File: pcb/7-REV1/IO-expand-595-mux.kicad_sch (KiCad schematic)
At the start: 58 parts, among them U10 LM358_DFN, U11 LM358_DFN, U12 LM358_DFN, U13 LM358_DFN, U2 74LVC8T245BQ, U402 CD4067, U503 74HCT245BQ, U9 LM358_DFN

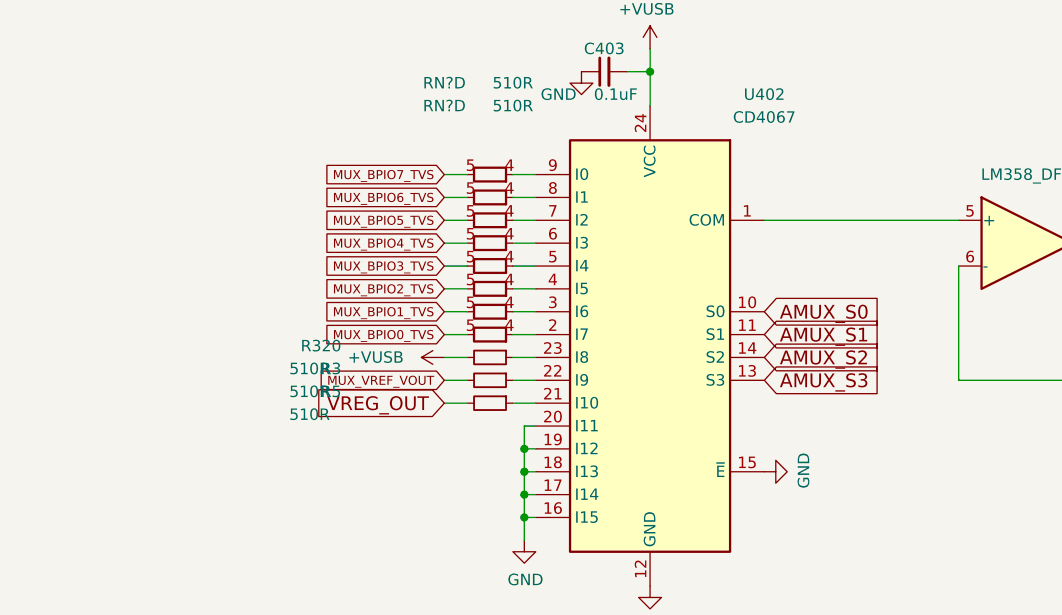
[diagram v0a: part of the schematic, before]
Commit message: Move CURRENT_DETECT back to AMUX
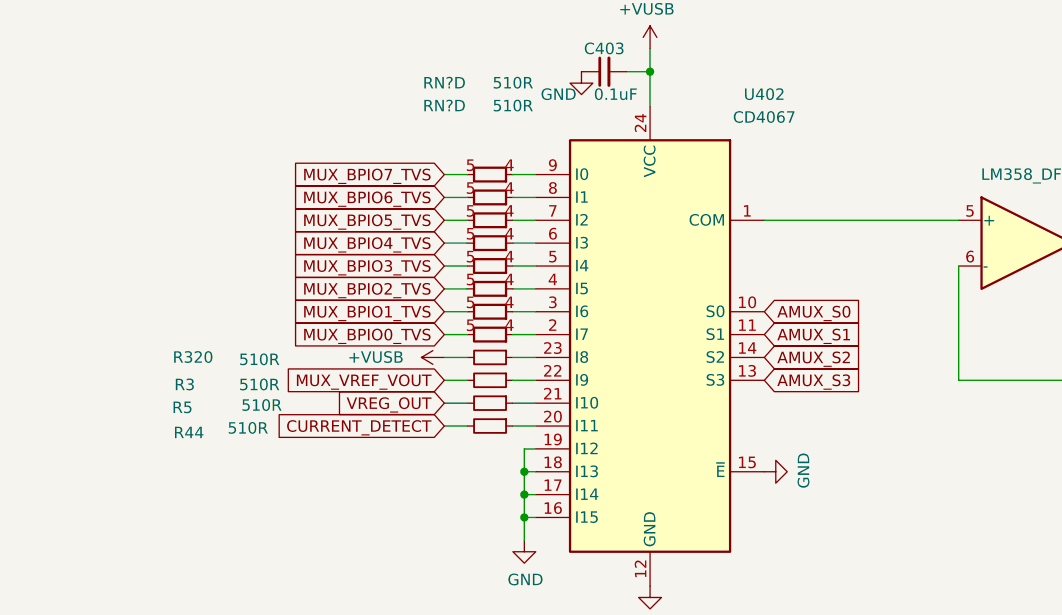
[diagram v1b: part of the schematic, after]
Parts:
- added R44: 510R, Resistor_SMD:R_0402_1005Metric, symbol Device:R_Small
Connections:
- net GND: no longer U402.20 (I11)
- new net: R44.1, U402.20 (I11)
- new net CURRENT_DETECT: R44.2
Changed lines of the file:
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@@
 	)
 	(junction
-		(at 246.38 170.18)
-		(diameter 0)
-		(color 0 0 0 0)
-	)
-	(junction
 		(at 76.2 175.26)
 		(diameter 0)
@@
 	(wire
 		(pts
+			(xy 237.49 167.64) (xy 240.03 167.64)
+		)
+		(stroke
+			(width 0)
+			(type default)
+		)
+	)
+	(wire
+		(pts
 			(xy 237.49 142.24) (xy 240.03 142.24)
 		)
@@
 	(wire
 		(pts
-			(xy 246.38 167.64) (xy 246.38 170.18)
-		)
-		(stroke
-			(width 0)
-			(type default)
-		)
-	)
-	(wire
-		(pts
 			(xy 245.11 162.56) (xy 247.65 162.56)
 		)
@@
 	(wire
 		(pts
-			(xy 246.38 167.64) (xy 247.65 167.64)
-		)
-		(stroke
-			(width 0)
-			(type default)
-		)
-	)
-	(wire
-		(pts
 			(xy 41.91 78.74) (xy 60.96 78.74)
 		)
@@
 	(wire
 		(pts
+			(xy 245.11 167.64) (xy 247.65 167.64)
+		)
+		(stroke
+			(width 0)
+			(type default)
+		)
+	)
+	(wire
+		(pts
 			(xy 142.24 121.92) (xy 157.48 121.92)
 		)
@@
 		(effects
 			(font
-				(size 1 1)
+				(size 1.27 1.27)
 			)
 			(justify right)
@@
 		(effects
 			(font
-				(size 1.524 1.524)
+				(size 1.27 1.27)
 			)
 			(justify left)
@@
 		(effects
 			(font
-				(size 1.524 1.524)
+				(size 1.27 1.27)
 			)
 			(justify left)
@@
 		(effects
 			(font
-				(size 1 1)
+				(size 1.27 1.27)
 			)
 			(justify right)
@@
 		(effects
 			(font
-				(size 1 1)
+				(size 1.27 1.27)
 			)
 			(justify right)
@@
 		(effects
 			(font
-				(size 1.524 1.524)
+				(size 1.27 1.27)
 			)
 			(justify right)
@@
 		(effects
 			(font
-				(size 1 1)
+				(size 1.27 1.27)
 			)
 			(justify right)
@@
 		(effects
 			(font
-				(size 1 1)
+				(size 1.27 1.27)
 			)
 			(justify right)
@@
 		(effects
 			(font
-				(size 1 1)
+				(size 1.27 1.27)
 			)
 			(justify right)
@@
 		)
 	)
+	(global_label "CURRENT_DETECT"
+		(shape input)
+		(at 237.49 167.64 180)
+		(fields_autoplaced yes)
+		(effects
+			(font
+				(size 1.27 1.27)
+			)
+			(justify right)
+		)
+		(property "Intersheetrefs" "${INTERSHEET_REFS}"
+			(at 218.8306 167.64 0)
+			(effects
+				(font
+					(size 1.27 1.27)
+				)
+				(justify right)
+				(hide yes)
+			)
+		)
+	)
 	(global_label "BPIO7_TVS"
 		(shape input)
@@
 		(effects
 			(font
-				(size 1 1)
+				(size 1.27 1.27)
 			)
 			(justify right)
@@
 		(effects
 			(font
-				(size 1 1)
+				(size 1.27 1.27)
 			)
 			(justify right)
@@
 		(effects
 			(font
-				(size 1.524 1.524)
+				(size 1.27 1.27)
 			)
 			(justify left)
@@
 		(effects
 			(font
-				(size 1 1)
+				(size 1.27 1.27)
 			)
 			(justify right)
@@
 		(effects
 			(font
-				(size 1.524 1.524)
+				(size 1.27 1.27)
 			)
 			(justify left)
@@
 		(dnp no)
 		(property "Reference" "R320"
-			(at 226.06 158.75 90)
+			(at 211.836 160.02 90)
 			(effects
 				(font
@@
 		)
 		(property "Value" "510R"
-			(at 224.79 161.29 90)
+			(at 219.202 160.274 90)
 			(effects
 				(font
@@
 	)
 	(symbol
+		(lib_id "Device:R_Small")
+		(at 242.57 167.64 270)
+		(unit 1)
+		(exclude_from_sim no)
+		(in_bom yes)
+		(on_board yes)
+		(dnp no)
+		(property "Reference" "R44"
+			(at 210.82 168.402 90)
+			(effects
+				(font
+					(size 1.27 1.27)
+				)
+				(justify right)
+			)
+		)
+		(property "Value" "510R"
+			(at 217.932 167.894 90)
+			(effects
+				(font
+					(size 1.27 1.27)
+				)
+				(justify right)
+			)
+		)
+		(property "Footprint" "Resistor_SMD:R_0402_1005Metric"
+			(at 242.57 167.64 0)
+			(effects
+				(font
+					(size 1.27 1.27)
+				)
+				(hide yes)
+			)
+		)
+		(property "Datasheet" "~"
+			(at 242.57 167.64 0)
+			(effects
+				(font
+					(size 1.27 1.27)
+				)
+				(hide yes)
+			)
+		)
+		(property "Description" ""
+			(at 242.57 167.64 0)
+			(effects
+				(font
+					(size 1.27 1.27)
+				)
+				(hide yes)
+			)
+		)
+		(property "RMB" "0.004864"
+			(at 242.57 167.64 0)
+			(effects
+				(font
+					(size 1.27 1.27)
+				)
+				(hide yes)
+			)
+		)
+		(property "Supplier" "https://item.szlcsc.com/61542.html"
+			(at 242.57 167.64 0)
+			(effects
+				(font
+					(size 1.27 1.27)
+				)
+				(hide yes)
+			)
+		)
+		(pin "1"
+		)
+		(pin "2"
+		)
+		(instances
+			(project "7-REV1"
+				(path "/1f56410a-eaac-4444-b0f7-cfd3531e22ac/00000000-0000-0000-0000-000060e58ecc"
+					(reference "R44")
+					(unit 1)
+				)
+			)
+		)
+	)
+	(symbol
 		(lib_id "Amplifier_Operational:LM358_DFN")
 		(at 149.86 177.8 0)
@@
 		(dnp no)
 		(property "Reference" "R3"
-			(at 226.06 161.29 90)
+			(at 209.804 163.068 90)
 			(effects
 				(font
@@
 		)
 		(property "Value" "510R"
-			(at 224.79 163.83 90)
+			(at 219.202 163.068 90)
 			(effects
 				(font
@@
 		(dnp no)
 		(property "Reference" "R5"
-			(at 226.06 163.83 90)
+			(at 209.55 165.608 90)
 			(effects
 				(font
@@
 		)
 		(property "Value" "510R"
-			(at 224.79 166.37 90)
+			(at 219.456 165.354 90)
 			(effects
 				(font

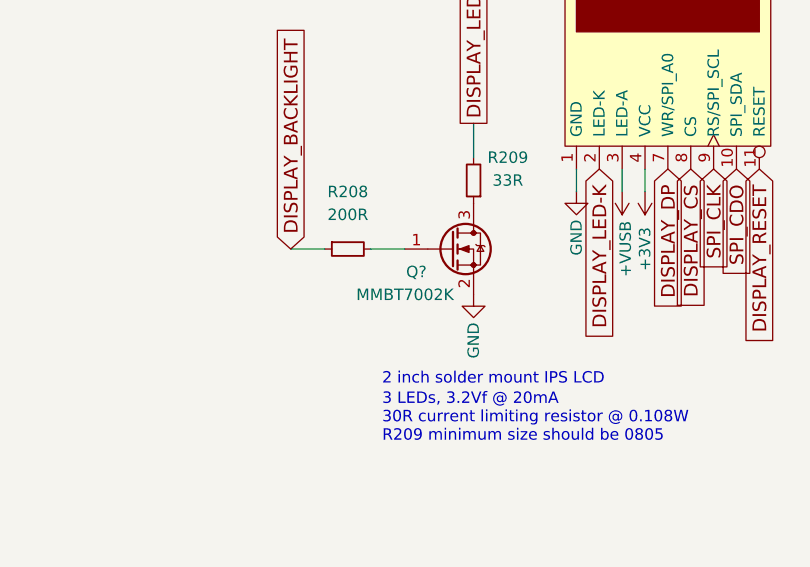
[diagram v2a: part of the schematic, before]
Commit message: replace one more MMBT7002K in SOT-23 with 2N7002T in SOT-523 (display led backlight)
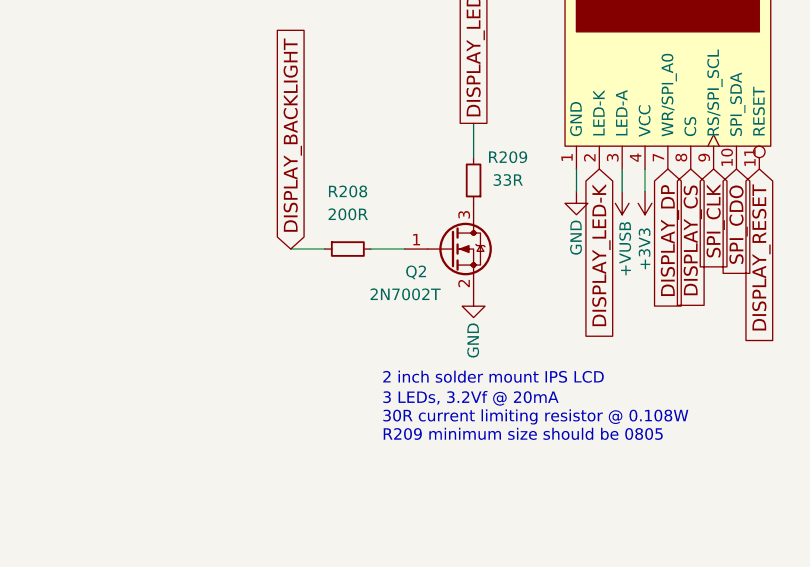
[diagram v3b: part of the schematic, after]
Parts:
- removed Q?: MMBT7002K, Package_TO_SOT_SMD:SOT-23, symbol Transistor_FET:BSS138
- added Q2: 2N7002T, Package_TO_SOT_SMD:SOT-523, symbol Transistor_FET:BSS138
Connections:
- net GND: now also Q2.2 (S)
- net at R208.2: now also Q2.1 (G)
- net at R209.1: now also Q2.3 (D)
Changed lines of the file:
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@@
-	)
-	(symbol
-		(lib_id "Transistor_FET:BSS138")
-		(at 344.17 69.85 0)
-		(unit 1)
-		(exclude_from_sim no)
-		(in_bom yes)
-		(on_board yes)
-		(dnp no)
-		(property "Reference" "Q?"
-			(at 340.36 72.39 0)
-			(effects
-				(font
-					(size 1.27 1.27)
-				)
-			)
-		)
-		(property "Value" "MMBT7002K"
-			(at 339.09 74.93 0)
-			(effects
-				(font
-					(size 1.27 1.27)
-				)
-			)
-		)
-		(property "Footprint" "Package_TO_SOT_SMD:SOT-23"
-			(at 349.25 71.755 0)
-			(effects
-				(font
-					(size 1.27 1.27)
-					(italic yes)
-				)
-				(justify left)
-				(hide yes)
-			)
-		)
-		(property "Datasheet" "https://www.fairchildsemi.com/datasheets/BS/BSS138.pdf"
-			(at 344.17 69.85 0)
-			(effects
-				(font
-					(size 1.27 1.27)
-				)
-				(justify left)
-				(hide yes)
-			)
-		)
-		(property "Description" ""
-			(at 344.17 69.85 0)
-			(effects
-				(font
-					(size 1.27 1.27)
-				)
-				(hide yes)
-			)
-		)
-		(property "RMB" "0.140017"
-			(at 344.17 69.85 0)
-			(effects
-				(font
-					(size 1.27 1.27)
-				)
-				(hide yes)
-			)
-		)
-		(property "Supplier" "https://item.szlcsc.com/544697.html"
-			(at 344.17 69.85 0)
-			(effects
-				(font
-					(size 1.27 1.27)
-				)
-				(hide yes)
-			)
-		)
-		(pin "1"
-		)
-		(pin "2"
-		)
-		(pin "3"
-		)
-		(instances
-			(project "REV0"
-				(path "/1f56410a-eaac-4444-b0f7-cfd3531e22ac/00000000-0000-0000-0000-00005f46fad3"
-					(reference "Q?")
-					(unit 1)
-				)
-				(path "/1f56410a-eaac-4444-b0f7-cfd3531e22ac/00000000-0000-0000-0000-000060e58ecc"
-					(reference "Q202")
-					(unit 1)
-				)
-			)
-		)
 	)
 	(symbol
@@
 					(unit 1)
 				)
+			)
+		)
+	)
+	(symbol
+		(lib_id "Transistor_FET:BSS138")
+		(at 344.17 69.85 0)
+		(unit 1)
+		(exclude_from_sim no)
+		(in_bom yes)
+		(on_board yes)
+		(dnp no)
+		(property "Reference" "Q2"
+			(at 340.36 72.39 0)
+			(effects
+				(font
+					(size 1.27 1.27)
+				)
+			)
+		)
+		(property "Value" "2N7002T"
+			(at 339.09 74.93 0)
+			(effects
+				(font
+					(size 1.27 1.27)
+				)
+			)
+		)
+		(property "Footprint" "Package_TO_SOT_SMD:SOT-523"
+			(at 349.25 71.755 0)
+			(effects
+				(font
+					(size 1.27 1.27)
+					(italic yes)
+				)
+				(justify left)
+				(hide yes)
+			)
+		)
+		(property "Datasheet" "https://www.onsemi.com/download/data-sheet/pdf/2n7002t-d.pdf"
+			(at 344.17 69.85 0)
+			(effects
+				(font
+					(size 1.27 1.27)
+				)
+				(justify left)
+				(hide yes)
+			)
+		)
+		(property "Description" ""
+			(at 344.17 69.85 0)
+			(effects
+				(font
+					(size 1.27 1.27)
+				)
+				(hide yes)
+			)
+		)
+		(property "RMB" "0.140017"
+			(at 344.17 69.85 0)
+			(effects
+				(font
+					(size 1.27 1.27)
+				)
+				(hide yes)
+			)
+		)
+		(property "Supplier" "https://item.szlcsc.com/544697.html"
+			(at 344.17 69.85 0)
+			(effects
+				(font
+					(size 1.27 1.27)
+				)
+				(hide yes)
+			)
+		)
+		(pin "1"
+		)
+		(pin "2"
+		)
+		(pin "3"
+		)
+		(instances
+			(project "7-REV1"
+				(path "/1f56410a-eaac-4444-b0f7-cfd3531e22ac/00000000-0000-0000-0000-000060e58ecc"
+					(reference "Q2")
+					(unit 1)
+				)

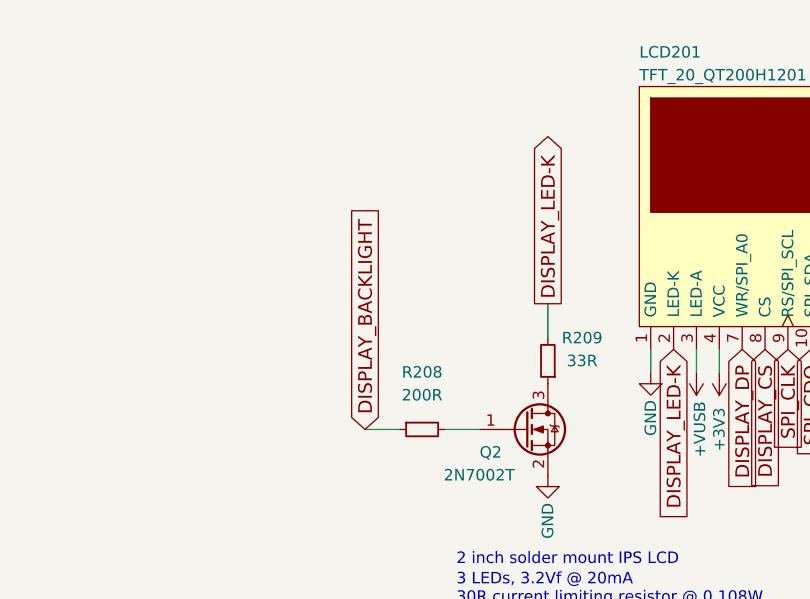
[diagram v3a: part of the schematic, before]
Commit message: remove gate series resistor for the display backlight - it is unnecessary
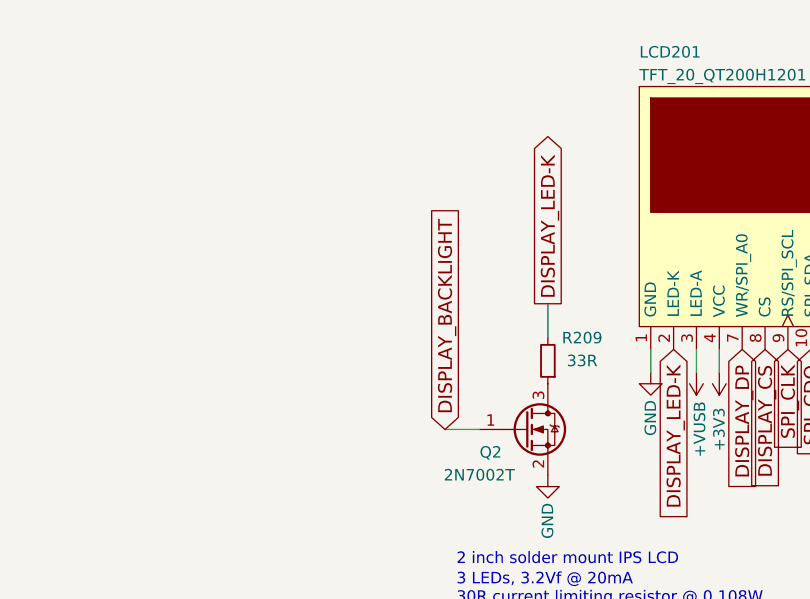
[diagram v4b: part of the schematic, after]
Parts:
- removed R208: 200R, Resistor_SMD:R_0402_1005Metric, symbol Device:R_Small
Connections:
- net DISPLAY_BACKLIGHT: now also Q2.1 (G)
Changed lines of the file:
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@@
 	(wire
 		(pts
-			(xy 330.2 69.85) (xy 326.39 69.85)
-		)
-		(stroke
-			(width 0)
-			(type default)
-		)
-	)
-	(wire
-		(pts
 			(xy 106.68 233.68) (xy 100.33 233.68)
 		)
@@
 	(global_label "DISPLAY_BACKLIGHT"
 		(shape input)
-		(at 326.39 69.85 90)
+		(at 335.28 69.85 90)
 		(effects
 			(font
@@
 		)
 		(property "Intersheetrefs" "${INTERSHEET_REFS}"
-			(at 326.39 69.85 0)
+			(at 335.28 69.85 0)
 			(effects
 				(font
@@
 					(unit 1)
 				)
-			)
-		)
-	)
-	(symbol
-		(lib_id "Device:R_Small")
-		(at 332.74 69.85 90)
-		(mirror x)
-		(unit 1)
-		(exclude_from_sim no)
-		(in_bom yes)
-		(on_board yes)
-		(dnp no)
-		(property "Reference" "R208"
-			(at 332.74 63.5 90)
-			(effects
-				(font
-					(size 1.27 1.27)
-				)
-			)
-		)
-		(property "Value" "200R"
-			(at 332.74 66.04 90)
-			(effects
-				(font
-					(size 1.27 1.27)
-				)
-			)
-		)
-		(property "Footprint" "Resistor_SMD:R_0402_1005Metric"
-			(at 332.74 69.85 0)
-			(effects
-				(font
-					(size 1.27 1.27)
-				)
-				(hide yes)
-			)
-		)
-		(property "Datasheet" "~"
-			(at 332.74 69.85 0)
-			(effects
-				(font
-					(size 1.27 1.27)
-				)
-				(hide yes)
-			)
-		)
-		(property "Description" ""
-			(at 332.74 69.85 0)
-			(effects
-				(font
-					(size 1.27 1.27)
-				)
-				(hide yes)
-			)
-		)
-		(property "RMB" "0.005749"
-			(at 332.74 69.85 0)
-			(effects
-				(font
-					(size 1.27 1.27)
-				)
-				(hide yes)
-			)
-		)
-		(property "Supplier" "https://item.szlcsc.com/61543.html"
-			(at 332.74 69.85 0)
-			(effects
-				(font
-					(size 1.27 1.27)
-				)
-				(hide yes)
-			)
-		)
-		(pin "1"
-		)
-		(pin "2"
-		)
-		(instances
-			(project "REV0"
-				(path "/1f56410a-eaac-4444-b0f7-cfd3531e22ac/00000000-0000-0000-0000-000060e58ecc"
-					(reference "R208")
-					(unit 1)
-				)

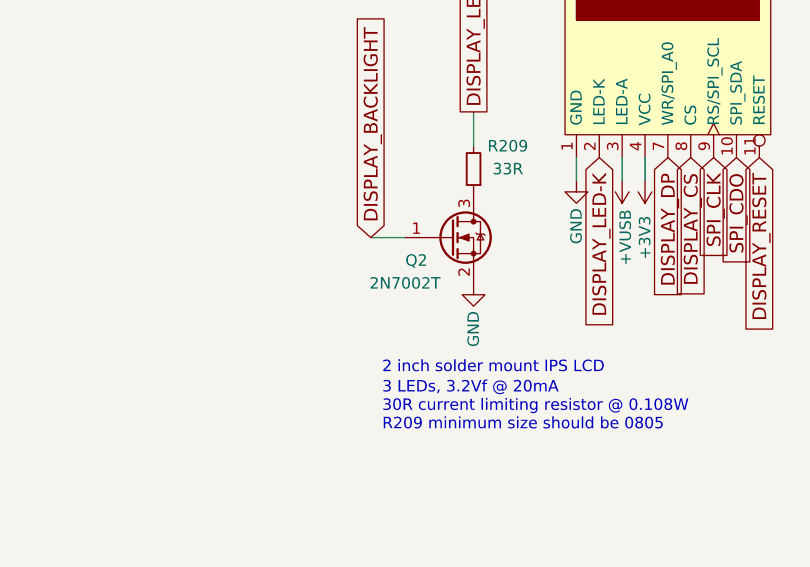
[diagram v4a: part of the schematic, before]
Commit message: specify part numbers and manufacturers in more detail - 10µF / 0805 caps - 2N7002KT fets
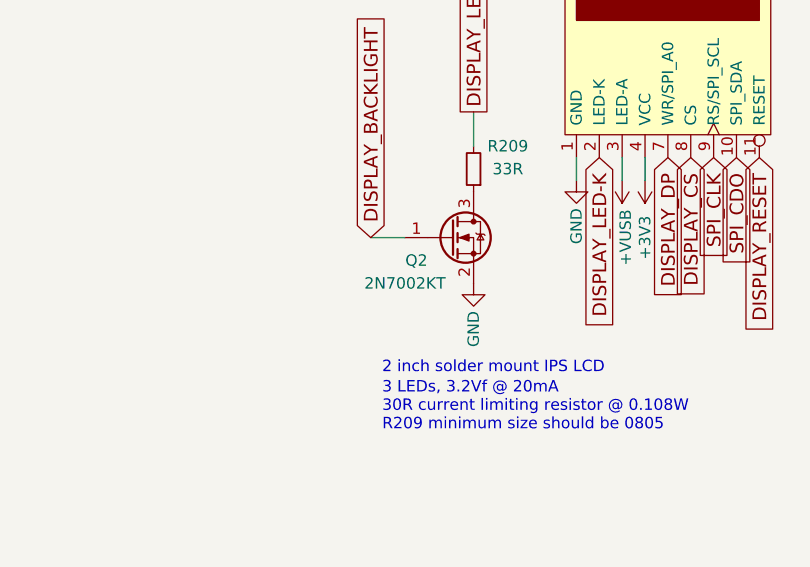
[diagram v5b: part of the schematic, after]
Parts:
- Q2: value 2N7002T -> 2N7002KT; MANUFACTURER (none) -> CBI
